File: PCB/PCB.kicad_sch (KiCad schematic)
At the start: 60 parts

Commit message: pcb edits
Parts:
- removed Q?: BD441, Package_TO_SOT_THT:TO-126-3_Vertical, symbol Transistor_BJT:BD441
- added D5: LED_RGBA, LED_THT:LED_D5.0mm-4_RGB, symbol Device:LED_RGBA
- added H1, H2: MountingHole, MountingHole:MountingHole_3.2mm_M3_Pad_Via, symbol Mechanical:MountingHole
- added TP10: BatteryPlusPad, TestPoint:TestPoint_THTPad_D2.5mm_Drill1.2mm, symbol Connector:TestPoint
- added TP9: BatteryMinusPad, TestPoint:TestPoint_THTPad_D2.5mm_Drill1.2mm, symbol Connector:TestPoint
- D2: renamed from D?; footprint Diode_THT:D_DO-35_SOD27_P7.62mm_Horizontal -> Diode_SMD:D_1206_3216Metric
- D3, D4: renamed from D?; footprint Diode_THT:D_DO-41_SOD81_P10.16mm_Horizontal -> Diode_SMD:D_1206_3216Metric
- J1: renamed from J?; footprint (none) -> Connector_USB:USB_Micro-B_Molex_47346-0001
- Q1, Q2: renamed from Q?; footprint Package_TO_SOT_THT:TO-92_Inline -> Package_TO_SOT_SMD:SC-82AA_Handsoldering
- Q4: renamed from Q?; footprint Package_TO_SOT_THT:TO-126-3_Vertical -> Package_TO_SOT_SMD:SC-82AA_Handsoldering
- U4: renamed from U?; footprint (none) -> Package_SO:SOIC-8_3.9x4.9mm_P1.27mm
- gave numbers to parts that had none: 51

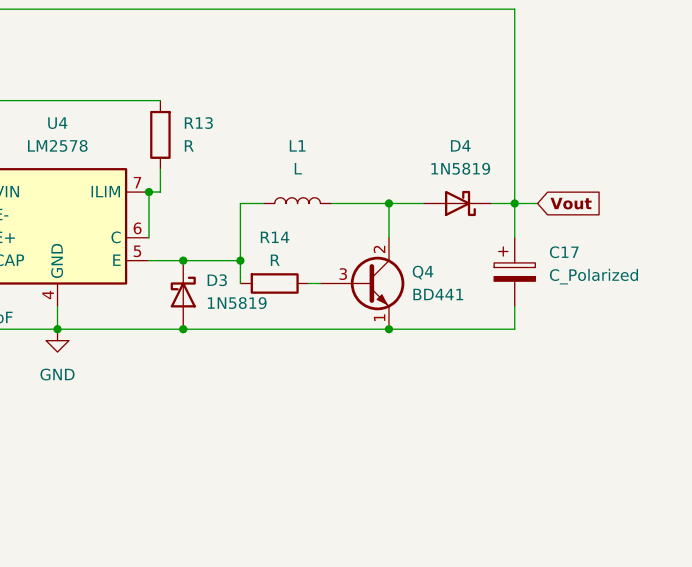
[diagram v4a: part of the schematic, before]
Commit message: pcb update (transistors)
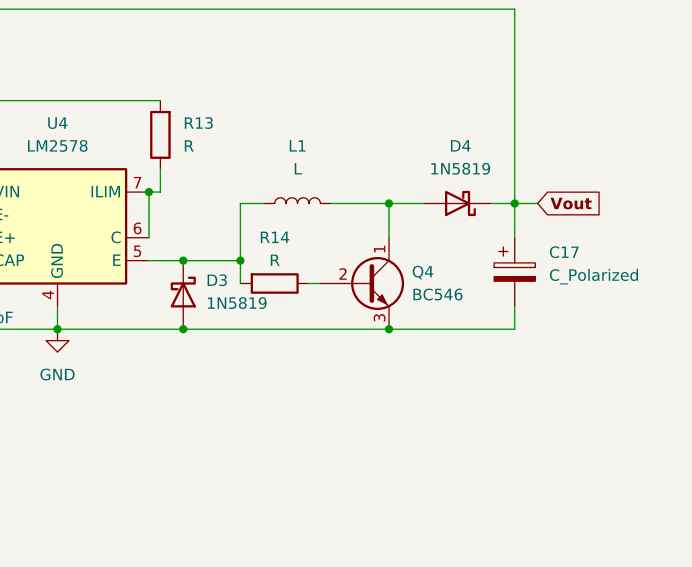
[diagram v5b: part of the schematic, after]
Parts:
- removed Q4: BD441, Package_TO_SOT_SMD:SC-82AA_Handsoldering, symbol Transistor_BJT:BD441
- added Q4: BC546, Package_TO_SOT_SMD:SC-82AA_Handsoldering, symbol Transistor_BJT:BC546
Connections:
- net GND: now also Q4.3 (E)
- net at D4.2 (A), L1.2: now also Q4.1 (C)
- net at R14.1: now also Q4.2 (B)

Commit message: progress on tp4056
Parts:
- added C? (x2): 10uF, symbol Device:C_Small
- added R?: 2k, symbol Device:R_Small_US
- H1, H2: symbol Mechanical:MountingHole -> Mechanical:MountingHole_Pad
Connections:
- net +BATT: now also TP10.1, U3.5 (BAT), C?.1
- net GND: now also H1.1, H2.1, TP9.1, U3.3 (GND), C?.1, C?.2, R?.1
- net at U3.2 (PROG): now also R?.2
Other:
- note added: "I2C address lower bit is set by SA0 (0x4A or 0x4B)"
- note removed: "I2C address lower bit is set by SA0 (0x4A or (0x4B)"
- moved on the sheet: C1, C10, C11, C12, C13, C14, C15, C16, C17, C2, C3, C4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

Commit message: most schematics done
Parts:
- removed C? (x2): 10uF, symbol Device:C_Small
- removed D5: LED_RGBA, LED_THT:LED_D5.0mm-4_RGB, symbol Device:LED_RGBA
- removed R3: 10k, symbol Device:R_Small_US
- removed R?: 2k, symbol Device:R_Small_US
- removed U3: TP4056, SOP127P600X175-9N, symbol TP4056:TP4056
- added C? (x2): 10uF, symbol Device:C_Small
- added C?: 1uF, symbol Device:C_Small
- added C? (x2): 12pf, symbol Device:C_Small
- added C?: 100nF, symbol Device:C_Small
- added D?: PowerLed, symbol Device:LED_Small
- added D?: LED_RGB, symbol Device:LED_RGBK
- added D?: Red, symbol Device:LED_Small
- added D?: Green, symbol Device:LED_Small
- added R? (x2): 3.3k, symbol Device:R_Small_US
- added R?: 470, symbol Device:R_Small_US
- added R? (x3): 10k, symbol Device:R_Small_US
- added R? (x2): 47k, symbol Device:R_Small_US
- added R?: 1k, symbol Device:R_Small_US
- added R?: 2k, symbol Device:R_Small_US
- added SW? (x2): SW_Push, symbol Switch:SW_Push
- added TP?: SCL_TP, symbol Connector:TestPoint
- added TP?: INT_TP, symbol Connector:TestPoint
- added TP?: GPIO0_TP, symbol Connector:TestPoint
- added TP?: SDA_TP, symbol Connector:TestPoint
- added TP?: ~{RESET}_TP, symbol Connector:TestPoint
- added U?: TP4056, SOP127P600X175-9N, symbol TP4056:TP4056
- added Y?: 32.768 kHz, symbol Device:Crystal_Small
- C1: value 22uF -> 10uF
- H1, H2: symbol Mechanical:MountingHole_Pad -> Mechanical:MountingHole
- TP1: value USB_D+ -> USB_D+_TP
- TP2: value USB_D- -> USB_D-_TP
- TP3: value InputVoltage -> InputVoltage_TP
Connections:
- net ~{BNO_RST is gone; now on net ~{BNO_RST}: R11.2, U5.11 (~{RST})
- net +3.3V: now also C?.2
- net +3V3: now also R?.1, R?.1, R?.1, SW?.2
- net +5V: now also C?.2, U?.4 (VCC), U?.8 (CE)
- net +BATT: now also C?.1, U?.5 (BAT)
- net BNO_INTERRUPT: now also U1.24 (IO4), TP?.1
- net GND: now also C?.1, C?.1, C?.1, C?.2, C?.2, C?.2, D?.1 (K), D?.4 (K), R?.1, R?.1, R?.1, R?.1, R?.2, SW?.1, U?.1 (TEMP), U?.3 (GND); no longer H1.1, H2.1
- net GPIO0: now also C?.2, R?.1, R?.2, TP?.1
- net I2C_SCL: now also U1.26 (IO20), R?.2, TP?.1
- net I2C_SDA: now also U1.34 (IO22), R?.2, TP?.1
- net Vin: now also R?.1
- net ~{RESET: now also TP?.1
- net XTAL_0: now reaches U1.12 (IO32)
- net XTAL_0: now also C?.1, Y?.2
- net XTAL_1: now reaches U1.13 (IO33)
- net XTAL_1: now also C?.1, Y?.1
- net ~{BNO_RST}: now reaches U1.17 (IO27)
- net RGB_BLUE: now reaches U1.18 (IO14)
- net RGB_BLUE: now also D?.3 (BA)
- net RGB_RED: now reaches U1.19 (IO12)
- net RGB_RED: now also D?.1 (RA)
- net RGB_GREEN: now reaches U1.20 (IO13)
- net RGB_GREEN: now also D?.2 (GA)
- net at U1.22 (IO2): now also R?.2
- net BATT_READ: now reaches U1.9 (I34)
- new net: D?.2 (A), R?.2
- new net: R?.1, SW?.1
- new net: D?.1 (K), R?.2 (x2)
- new net: R?.2, U?.2 (PROG)
- new net SESSION_BUTTON: R?.2, SW?.2
- new net ~{CHRG}: D?.2 (A), U?.7 (~{CHRG})
- new net ~{STDBY}: D?.2 (A), U?.6 (~{STDBY})
- no-connect marks 11 -> 12
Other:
- note added: "Battery Input"
- note added: "ESP32 Auto-Program Transistors"
- note added: "I2C Pullups"
- note added: "IO2 is held low for programming"
- note added: "Mounting Holes"
- note added: "RGB LED"
- note added: "Session Button"
- note added: "TP4056 Charge Controller"
- note removed: "Charge Controller"
- moved on the sheet: C1, C2, C3, C4, C5, C6, C7, D2, F1, Q1, Q2, Q3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

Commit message: more footprints!
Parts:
- C1, C10, C11, C15, C16, C2, C3, C4, C5, C6, C8, C9: footprint (none) -> Capacitor_SMD:C_0603_1608Metric
- C18, C19, C20, C23: renamed from C?; footprint (none) -> Capacitor_SMD:C_0603_1608Metric
- C21, C22: renamed from C?; footprint (none) -> Capacitor_SMD:C_1206_3216Metric
- C7: footprint (none) -> Capacitor_SMD:C_1206_3216Metric
- D5, D7, D8: renamed from D?; footprint (none) -> LED_SMD:LED_0805_2012Metric_Pad1.15x1.40mm_HandSolder
- D6: renamed from D?; footprint (none) -> LED_THT:LED_D5.0mm-4_RGB
- R1, R11, R15, R16, R2, R4, R5, R6, R7, R8: footprint (none) -> Resistor_SMD:R_0603_1608Metric
- R17, R18, R19, R20, R21, R24, R25, R3: renamed from R?; footprint (none) -> Resistor_SMD:R_0603_1608Metric
- R22, R23: renamed from R?; value 47k -> 470; footprint (none) -> Resistor_SMD:R_0603_1608Metric
- SW1: footprint (none) -> Button_Switch_SMD:SW_SPST_CK_RS282G05A3
- SW2, SW3: renamed from SW?; footprint (none) -> Button_Switch_SMD:SW_SPST_CK_RS282G05A3
- TP1, TP2, TP3: footprint (none) -> TestPoint:TestPoint_Pad_D1.0mm
- TP11, TP12, TP13, TP14, TP15: renamed from TP?; footprint (none) -> TestPoint:TestPoint_Pad_D1.0mm
- TP4: value TX -> TX_TP; footprint (none) -> TestPoint:TestPoint_Pad_D1.0mm
- TP5: value RX -> RX_TP; footprint (none) -> TestPoint:TestPoint_Pad_D1.0mm
- TP6: value RTS -> RTS_TP; footprint (none) -> TestPoint:TestPoint_Pad_D1.0mm
- TP7: value CTS -> CTS_TP; footprint (none) -> TestPoint:TestPoint_Pad_D1.0mm
- TP8: value DTR -> DTR_TP; footprint (none) -> TestPoint:TestPoint_Pad_D1.0mm
- U1: footprint MODULE_ESP32-PICO-MINI-02 -> ESP32:MODULE_ESP32-PICO-MINI-02
- U3: renamed from U?; footprint SOP127P600X175-9N -> TP4056:SOP127P600X175-9N
- U5: footprint IC_BNO080 -> BNO080:IC_BNO080
- Y1: footprint (none) -> Crystal:Crystal_SMD_EuroQuartz_EQ161-2Pin_3.2x1.5mm
- Y2: renamed from Y?; footprint (none) -> Crystal:Crystal_SMD_EuroQuartz_EQ161-2Pin_3.2x1.5mm
